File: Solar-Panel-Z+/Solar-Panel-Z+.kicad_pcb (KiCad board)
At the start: 6 copper layers, 48.4 x 48.4 mm, 63 parts, among them J1 FFC2B28-10-G, U1 Value, U2 TSL2561

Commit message: Exported Gerbers
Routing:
- net /coil: track 13159.2 -> 13524.9 mm
- net VSOLAR_FULL: track 22.0 -> 20.7 mm

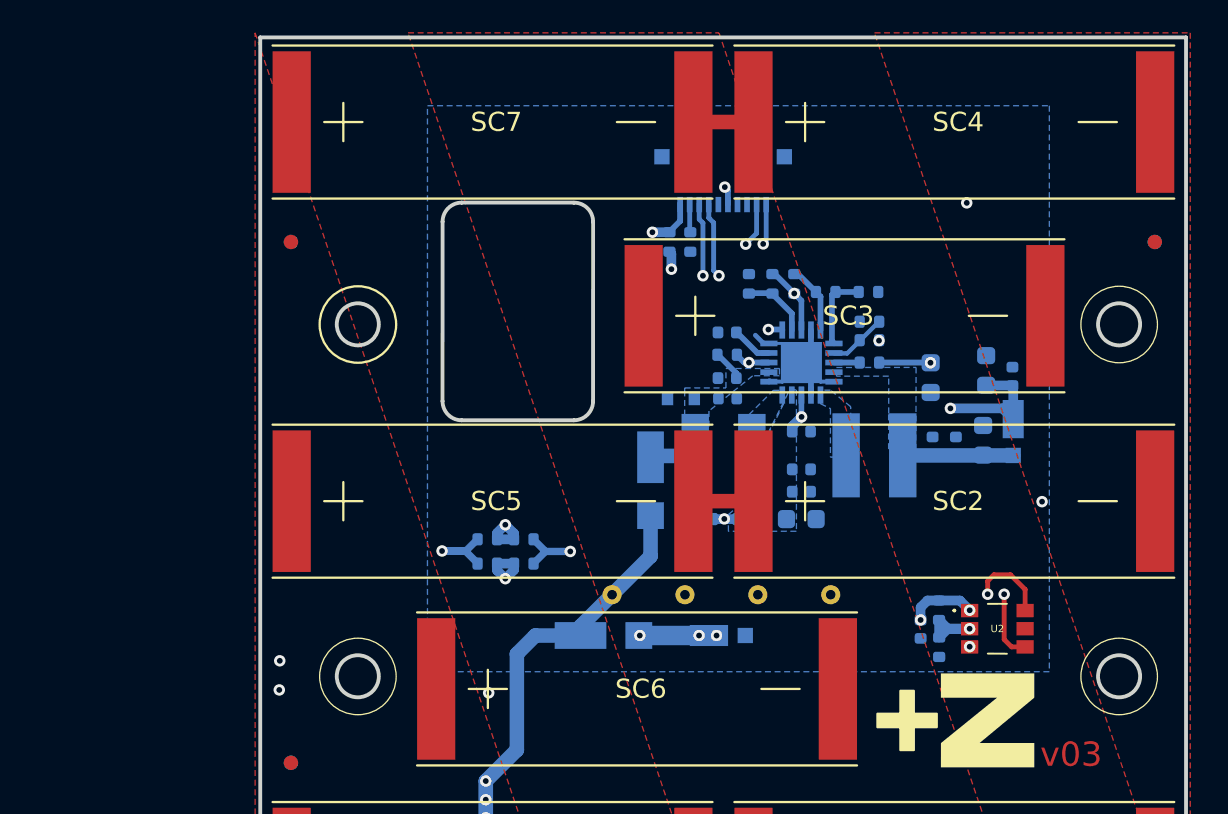
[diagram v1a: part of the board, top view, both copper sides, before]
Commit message: Stack architecture schematic updates / fixes
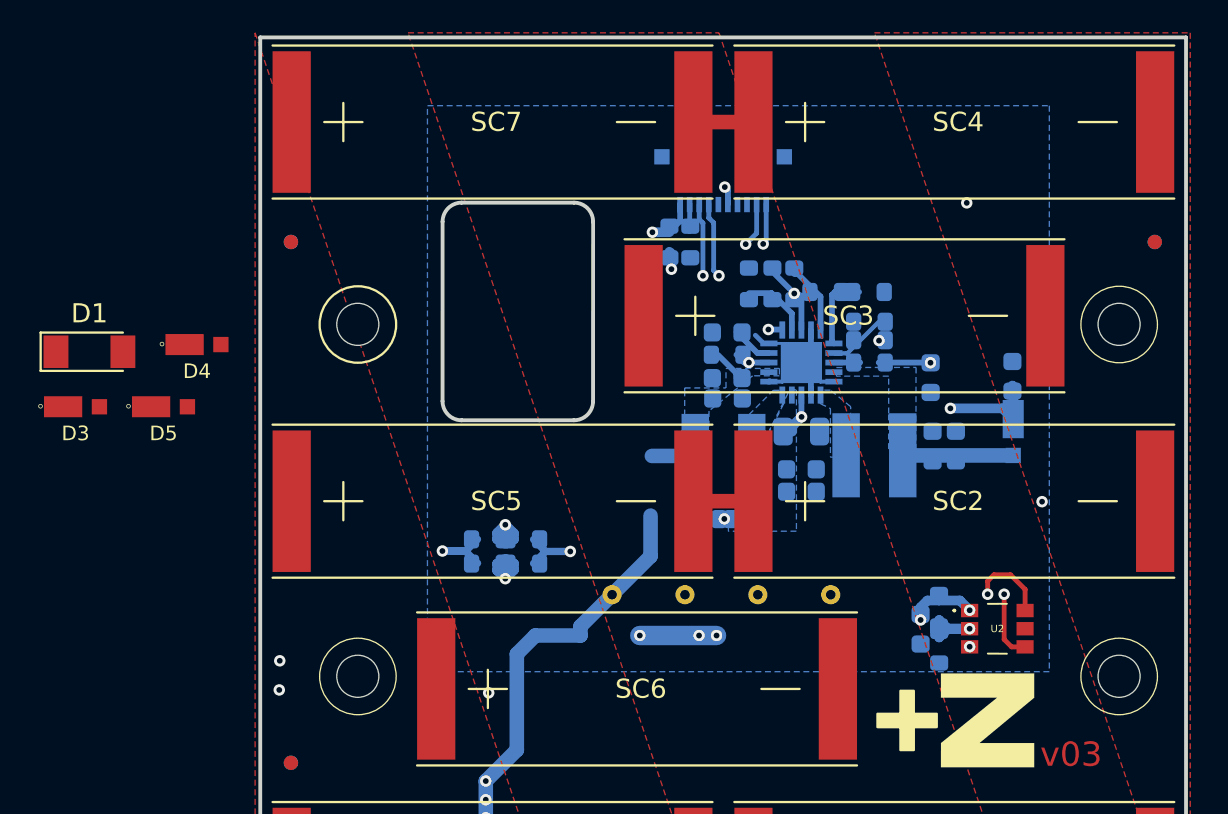
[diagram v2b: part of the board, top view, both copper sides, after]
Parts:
- removed the C11 at (156.6, 97.7)
- removed C12, C14: 100uF, Capacitor_SMD:C_0603_1608Metric
- added H1: MountingHole, MountingHole:MountingHole_2.2mm_M2_DIN965, F.Cu at (133.4, 87.6)
- added H2: MountingHole, MountingHole:MountingHole_2.2mm_M2_DIN965, F.Cu at (133.4, 106.0)
- added H3: MountingHole, MountingHole:MountingHole_2.2mm_M2_DIN965, F.Cu at (173.2, 106.0)
- added H4: MountingHole, MountingHole:MountingHole_2.2mm_M2_DIN965, F.Cu at (173.2, 87.6)
- C1: value 1.0uF -> 1uF; footprint Capacitor_SMD:C_0402_1005Metric -> Capacitor_SMD:C_0603_1608Metric
- C10, C2, C3, C4, C9: footprint Capacitor_SMD:C_0402_1005Metric -> Capacitor_SMD:C_0603_1608Metric
- C11: renamed from C13; footprint Capacitor_SMD:C_0402_1005Metric -> Capacitor_SMD:C_0603_1608Metric
- C5: value 0.1uF -> 100uF; footprint Capacitor_SMD:C_0402_1005Metric -> Capacitor_SMD:C_0805_2012Metric
- C6: value 100uF -> 1uF
- C7: value 22uF -> 4.7uF; footprint Capacitor_SMD:C_0402_1005Metric -> Capacitor_SMD:C_0603_1608Metric
- C8: value 4.7uF -> 22uF; footprint Capacitor_SMD:C_0402_1005Metric -> Capacitor_SMD:C_0603_1608Metric
- D1: value SDM20U40-7 -> BZV55B5V1; footprint Diode_SMD:D_SOD-523 -> Diode_SMD:D_MiniMELF; moved to F.Cu
- D3: moved to F.Cu
- D4, D5: value SBDiode -> MSS1P4-M3_89A; footprint solarpanels:SB Diode -> solarpanels:MICROSMP; moved to F.Cu
- R1, R10, R11, R12, R13, R14, R15, R16, R17, R18, R19, R2, R3, R4, R5, R6, R7, R8, R9: footprint Resistor_SMD:R_0402_1005Metric -> Resistor_SMD:R_0603_1608Metric
- U1: value Value -> BQ25570RGRR
- moved D3 35.8 mm to (118.6, 91.9)
- moved D1 31.0 mm to (119.4, 89.0), turned to 0 degrees
- moved D4 26.1 mm to (125.0, 88.6)
- moved D5 25.7 mm to (123.2, 91.9), turned to 0 degrees
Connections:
- D4 pad 1: VSOLAR_FULL -> Net-(D4-Pad1)
- D5 pad 2: VSOLAR_FULL -> Net-(D4-Pad1)
- SC5 pad 1: VSOLAR_FULL -> Net-(D4-Pad1)
- SC6 pad 1: VSOLAR_FULL -> Net-(D4-Pad1)
- SC7 pad 1: VSOLAR_FULL -> Net-(D4-Pad1)
- SC8 pad 1: VSOLAR_FULL -> Net-(D4-Pad1)
- TP1 pad 1: VSOLAR_FULL -> VSOLAR
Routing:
- net BATT_P: track 23.9 -> 56.2 mm, vias 1 -> 3
- net SDA1: track 30.9 -> 0.00 mm, vias 2 -> 0
- net VSOLAR_FULL: track 20.7 -> 0.00 mm, vias 3 -> 0
- net VSOLAR: track 3.89 -> 24.6 mm, vias 0 -> 3
- net Net-(R10-Pad2): track 8.94 -> 16.1 mm
- net /coil: track 13524.9 -> 13531.4 mm
- net Net-(SC1-Pad1): track 13.4 -> 9.43 mm, vias 3 -> 0
- net (no net): track 0.00 -> 4.01 mm, vias 0 -> 3
- net Net-(R7-Pad1): track 3.61 -> 0.00 mm
- net Net-(R5-Pad1): track 3.56 -> 0.00 mm
- net Net-(C4-Pad1): track 2.15 -> 0.00 mm
- net Net-(R14-Pad1): track 11.8 -> 14.0 mm
- net BATT_N: track 1.51 -> 0.00 mm
- net VBAT_OK: track 1.37 -> 0.00 mm
- net Net-(R10-Pad1): track 3.00 -> 4.37 mm
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- added copper zone on F.Cu, net Net-(D4-Pad1)
- removed copper zone on F.Cu, net VSOLAR_FULL
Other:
- outline, holes or cut-outs redrawn

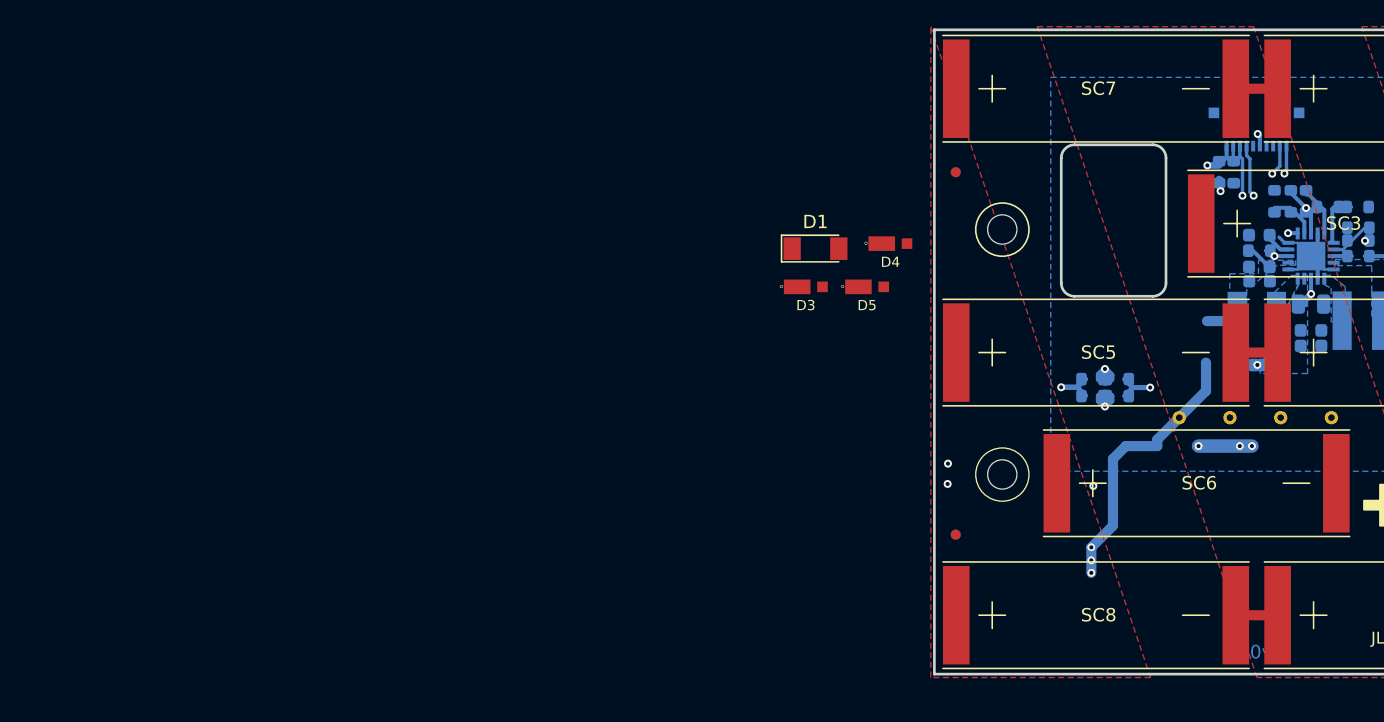
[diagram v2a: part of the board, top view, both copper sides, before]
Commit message: Added new edge cuts and connector
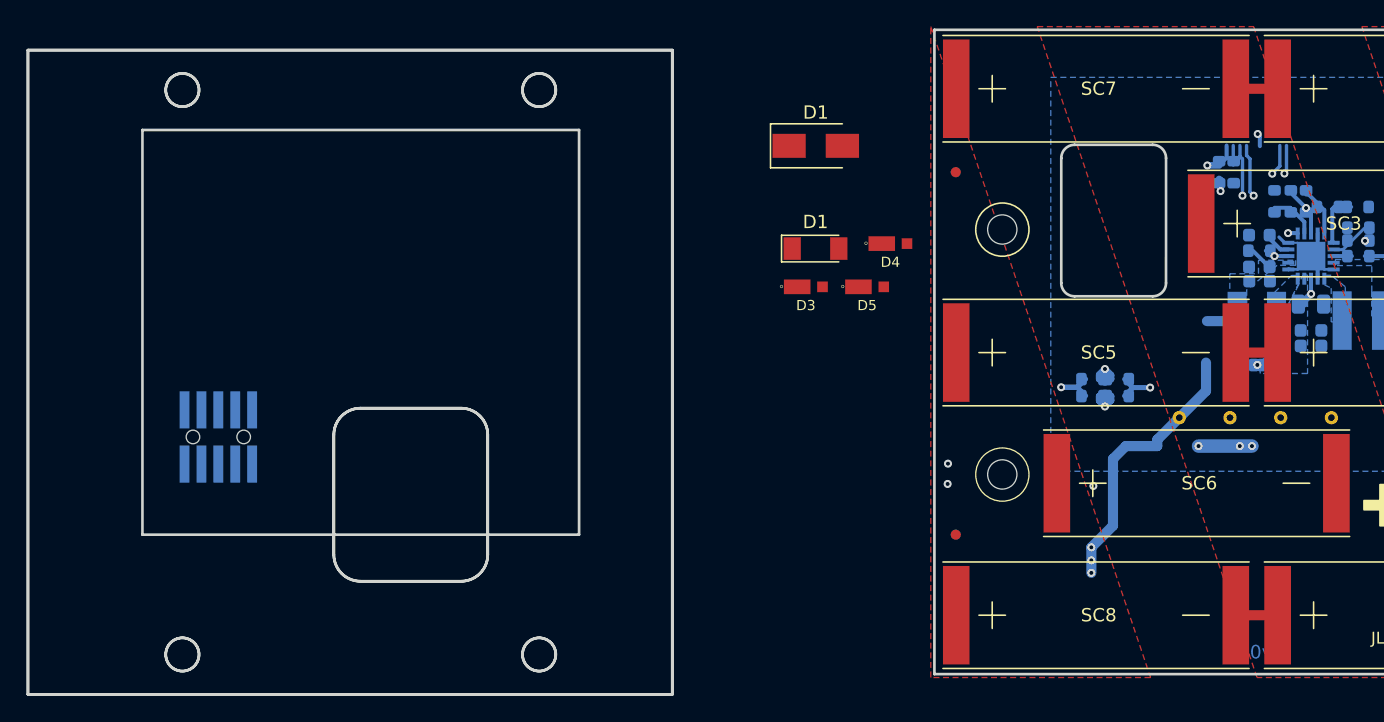
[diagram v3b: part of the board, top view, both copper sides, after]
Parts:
- added D1: SZ1SMA5918, Diode_SMD:D_SMA, F.Cu at (119.4, 81.3)
- J1: value FFC2B28-10-G -> TODO; footprint solarpanels:GCT_FFC2B28-10-G -> batteryboard:FTS-105-XX-YY-DV-A
- moved J1 81.3 mm to (74.5, 103.1), turned to 180 degrees
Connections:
- net SCL1 renamed SCL2
- net SDA1 renamed SDA2
- J1 pad 1: BATT_P -> +3V3
- J1 pad 10: COIL_P -> VUSB
- J1 pad 2: BATT_N -> GND
- J1 pad 5: BURN1 -> COIL_P
- J1 pad 6: +3V3 -> COIL_N
- J1 pad 7: GND -> BURN1
- J1 pad 8: GND -> BURN2
- J1 pad 9: COIL_N -> BATT_P
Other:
- board size 48.4 x 48.4 mm -> 116.5 x 49.9 mm

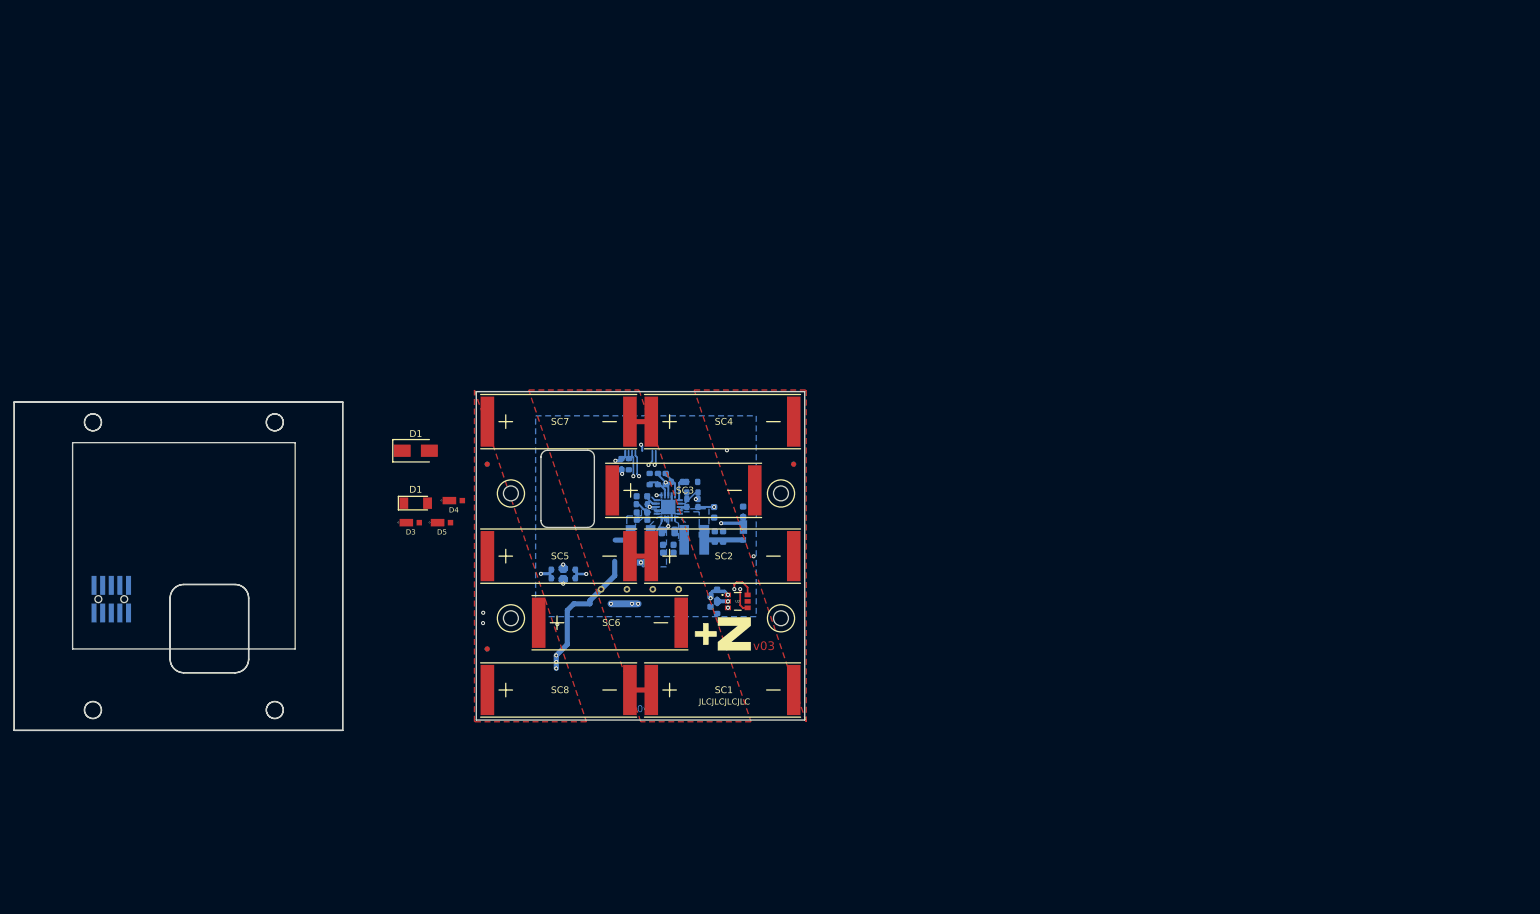
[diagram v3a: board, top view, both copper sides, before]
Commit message: Added 4 Layer Z+ board
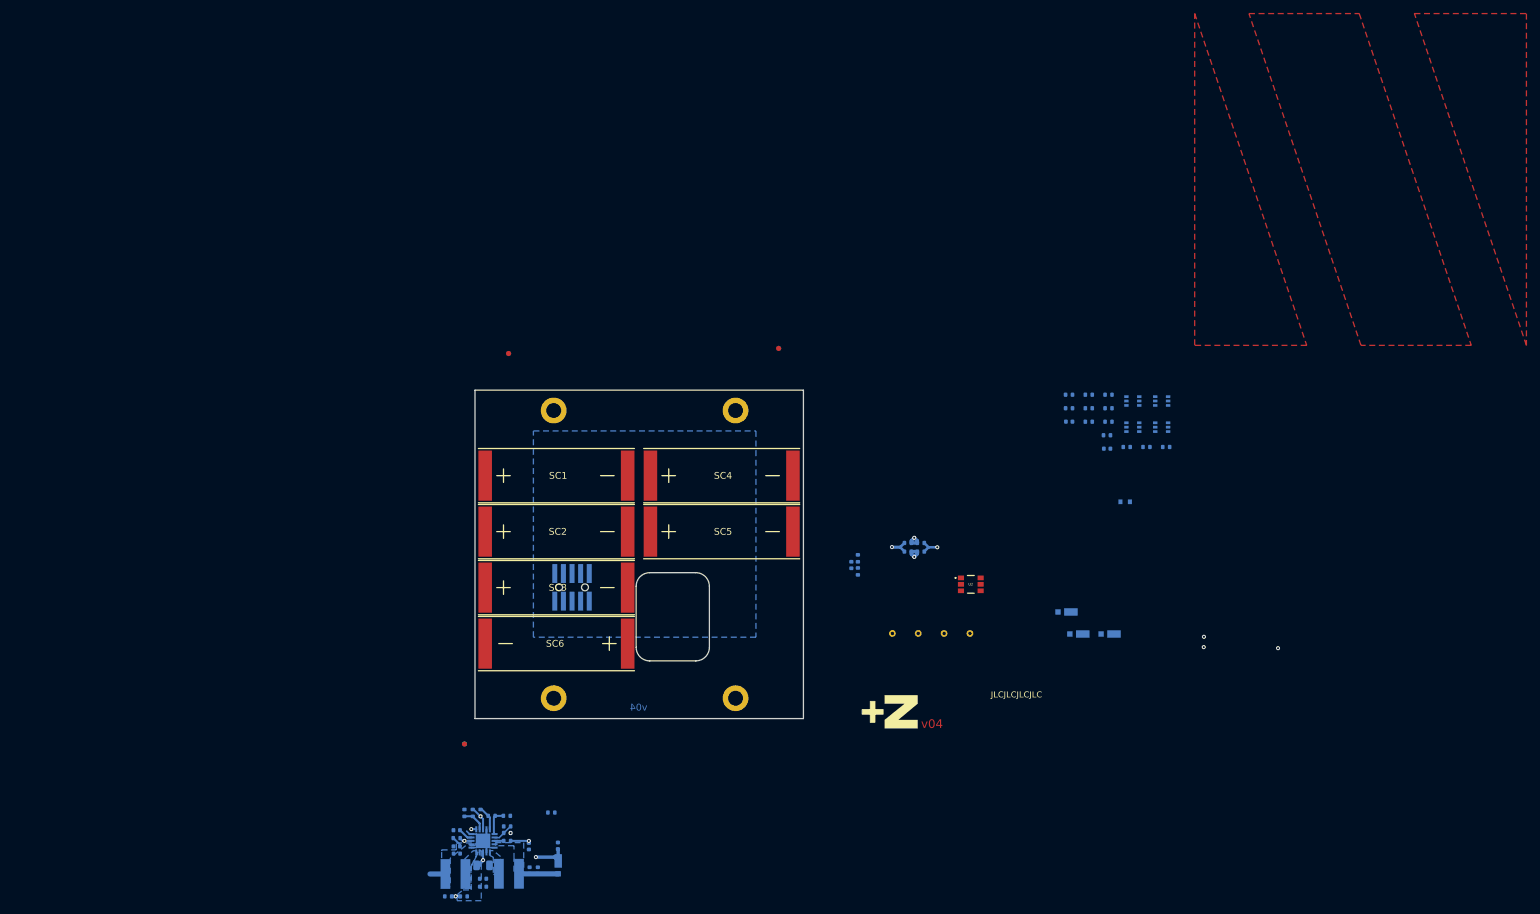
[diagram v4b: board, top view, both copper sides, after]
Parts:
- removed the D1 at (119.4, 89.0)
- removed the D1 at (119.4, 81.3)
- removed R4: 0, Resistor_SMD:R_0603_1608Metric
- removed the SC4 at (154.1, 77.0)
- removed SC7, SC8: SolarCell, solarpanels:KXOB25-05X3F
- added C12: 10nF, Capacitor_SMD:C_0402_1005Metric, B.Cu at (215.7, 77.0)
- added C13: 10nF, Capacitor_SMD:C_0402_1005Metric, B.Cu at (221.3, 81.0)
- added D1: SZMM5Z5V1T1G, Diode_SMD:D_SOD-523, B.Cu at (223.9, 88.8)
- added Q1: BSS138DWQ-7, Package_TO_SOT_SMD:SOT-363_SC-70-6, B.Cu at (229.3, 77.8)
- added Q2: MBT2222ADW1T1, Package_TO_SOT_SMD:SOT-363_SC-70-6, B.Cu at (225.0, 77.8)
- added Q3: BSS138DWQ-7, Package_TO_SOT_SMD:SOT-363_SC-70-6, B.Cu at (225.0, 74.0)
- added Q4: MBT2222ADW1T1, Package_TO_SOT_SMD:SOT-363_SC-70-6, B.Cu at (229.3, 74.0)
- added R20: 680, Resistor_SMD:R_0402_1005Metric, B.Cu at (224.1, 80.7)
- added R21: 100K, Resistor_SMD:R_0402_1005Metric, B.Cu at (230.0, 80.7)
- added R22: 0, Resistor_SMD:R_0402_1005Metric, B.Cu at (221.2, 79.0)
- added R23: 0, Resistor_SMD:R_0402_1005Metric, B.Cu at (218.6, 75.0)
- added R24: 10K, Resistor_SMD:R_0402_1005Metric, B.Cu at (221.5, 73.0)
- added R25: 10K, Resistor_SMD:R_0402_1005Metric, B.Cu at (215.6, 75.0)
- added R26: 200K, Resistor_SMD:R_0402_1005Metric, B.Cu at (215.6, 73.0)
- added R27: 680, Resistor_SMD:R_0402_1005Metric, B.Cu at (218.6, 77.0)
- added R28: 100K, Resistor_SMD:R_0402_1005Metric, B.Cu at (221.5, 77.0)
- added R29: 10K, Resistor_SMD:R_0402_1005Metric, B.Cu at (221.5, 75.0)
- added R30: 10K, Resistor_SMD:R_0402_1005Metric, B.Cu at (218.6, 73.0)
- added R31: 200K, Resistor_SMD:R_0402_1005Metric, B.Cu at (227.1, 80.7)
- added SC6: SolarCell, solarpanels:KXOB25-05X3F, F.Cu at (150.6, 109.7)
- C1, C10, C11, C2, C3, C4, C6, C7, C8, C9: footprint Capacitor_SMD:C_0603_1608Metric -> Capacitor_SMD:C_0402_1005Metric
- D3, D4, D5: moved to B.Cu
- H1, H2, H3, H4: footprint MountingHole:MountingHole_2.2mm_M2_DIN965 -> MountingHole:MountingHole_2.2mm_M2_DIN965_Pad
- J1: value TODO -> FTS-105-01-L-DV-A
- R1, R10, R11, R12, R13, R14, R15, R16, R17, R18, R19, R2, R3, R5, R6, R7, R8, R9: footprint Resistor_SMD:R_0603_1608Metric -> Resistor_SMD:R_0402_1005Metric
- moved D3 104.3 mm to (221.6, 108.3), turned to 180 degrees
- moved D5 95.2 mm to (217.0, 108.3), turned to 180 degrees
- moved D4 91.8 mm to (215.3, 105.0), turned to 180 degrees
- moved J1 67.9 mm to (142.4, 101.4)
- moved C10 56.3 mm to (137.4, 143.1)
- moved C5 56.3 mm to (129.3, 142.4)
- moved C6 56.3 mm to (136.0, 139.6)
- moved C7 56.3 mm to (129.3, 144.4)
- moved C8 56.3 mm to (136.1, 143.1)
- moved D2 56.3 mm to (140.4, 142.4)
- moved L1 56.3 mm to (125.2, 143.7)
- moved R11 56.3 mm to (132.8, 136.6)
- moved R15 56.3 mm to (124.2, 147.0)
- moved R16 56.3 mm to (126.4, 147.0)
- moved R5 56.3 mm to (127.8, 134.7)
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- renumbered SC5 to SC1, SC6 to SC2, SC1 to SC4, SC2 to SC5
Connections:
- C5 pad 1: /VBAT -> VBAT
- D4 pad 1: Net-(D4-Pad1) -> /VSOLAR_FULL
- D5 pad 2: Net-(D4-Pad1) -> /VSOLAR_FULL
- J1 pad 3: SDA2 -> BURN1
- J1 pad 4: SCL2 -> BURN2
- J1 pad 7: BURN1 -> SDA2
- J1 pad 8: BURN2 -> SCL2
- R3 pad 2: /VBAT -> VBAT
- SC1 pad 1: Net-(D4-Pad1) -> /VSOLAR_FULL
- SC2 pad 1: Net-(D4-Pad1) -> /VSOLAR_FULL
- SC3 pad 1: Net-(D3-Pad1) -> /VSOLAR_FULL
- SC3 pad 2: GND -> Net-(D3-Pad1)
- TP4 pad 1: BATT_P -> VBAT
- U1 pad 18: /VBAT -> VBAT
- U2 pad 4: SCL2 -> SCL_LS
- U2 pad 6: SDA2 -> SDA_LS
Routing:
- net /coil: track 13531.4 -> 7.26 mm, vias 5 -> 2
- net GND: track 9.38 -> 13526.1 mm
- net BATT_P: track 56.2 -> 0.00 mm, vias 3 -> 0
- net +3V3: track 49.5 -> 5.29 mm, vias 4 -> 1
- net SCL2: track 30.4 -> 0.00 mm, vias 2 -> 0
- net COIL_P: track 32.1 -> 2.83 mm, vias 2 -> 1
- net COIL_N: track 29.9 -> 2.78 mm, vias 2 -> 1
- net VSOLAR: track 24.6 -> 3.89 mm, vias 3 -> 0
- net /VBAT: track 16.1 -> 0.00 mm, vias 2 -> 0
- net Net-(R10-Pad2): track 16.1 -> 3.49 mm
- net Net-(R14-Pad1): track 14.0 -> 3.14 mm
- net Net-(D3-Pad1): track 9.43 -> 0.00 mm
- net VOUT_EN: track 12.6 -> 3.44 mm
- net Net-(R1-Pad1): track 4.47 -> 0.00 mm, vias 1 -> 0
- net (no net): track 4.01 -> 0.00 mm, vias 3 -> 0
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- added copper zone on F.Cu, net /VSOLAR_FULL
- removed copper zone on F.Cu, net Net-(D4-Pad1)
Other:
- board size 116.5 x 49.9 mm -> 48.4 x 48.4 mm
- board text added: "v04"
- board text removed: "1"
- board text removed: "v03"
